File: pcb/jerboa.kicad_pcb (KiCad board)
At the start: 2 copper layers, 72 parts, among them IC1 ADP1607, IC2 MAX-M8Q, IC3 Si4460, IC4 BGS12AL7, J1 CONN_01x02, J2 CONN_01x03, J3 CONN_01x02, J4 CONN_01x02, P1 SWD_TC, P2 434MHz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

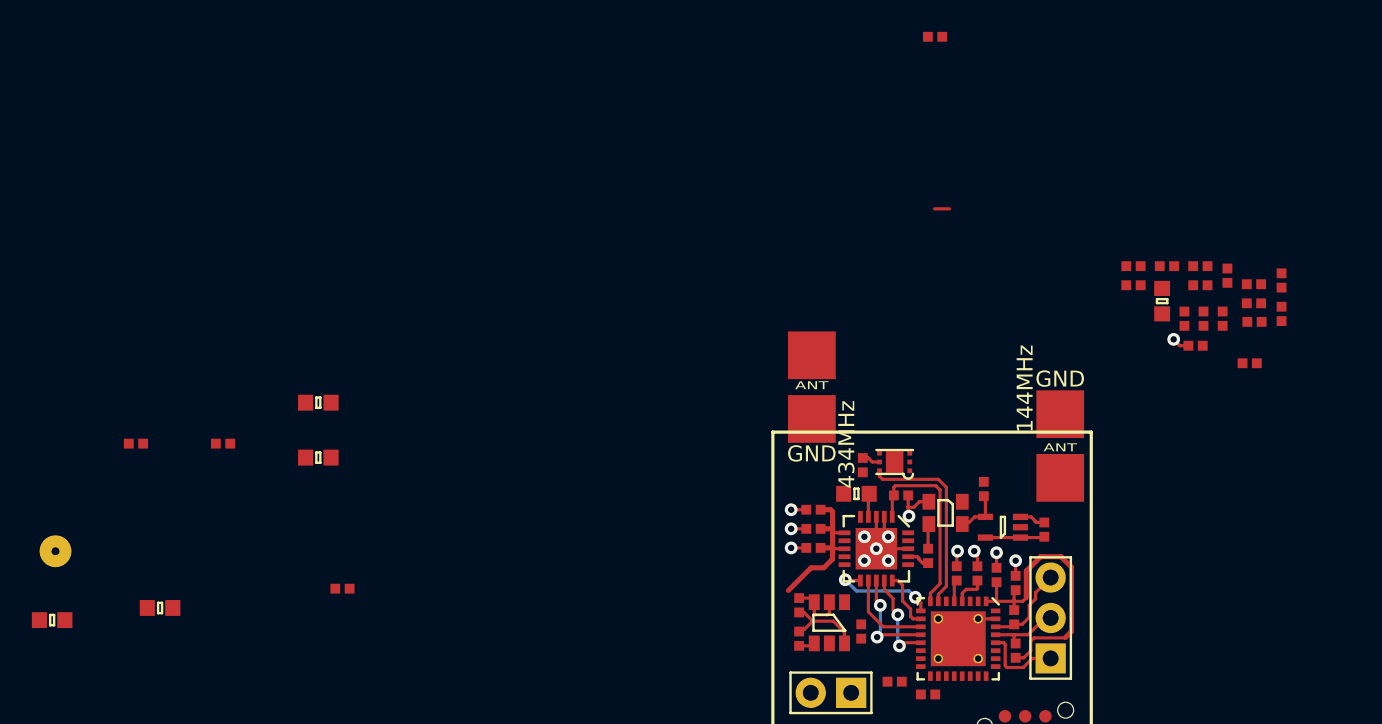
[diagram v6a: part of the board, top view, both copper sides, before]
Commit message: WIP: begin to place radio matching circuit on PCB
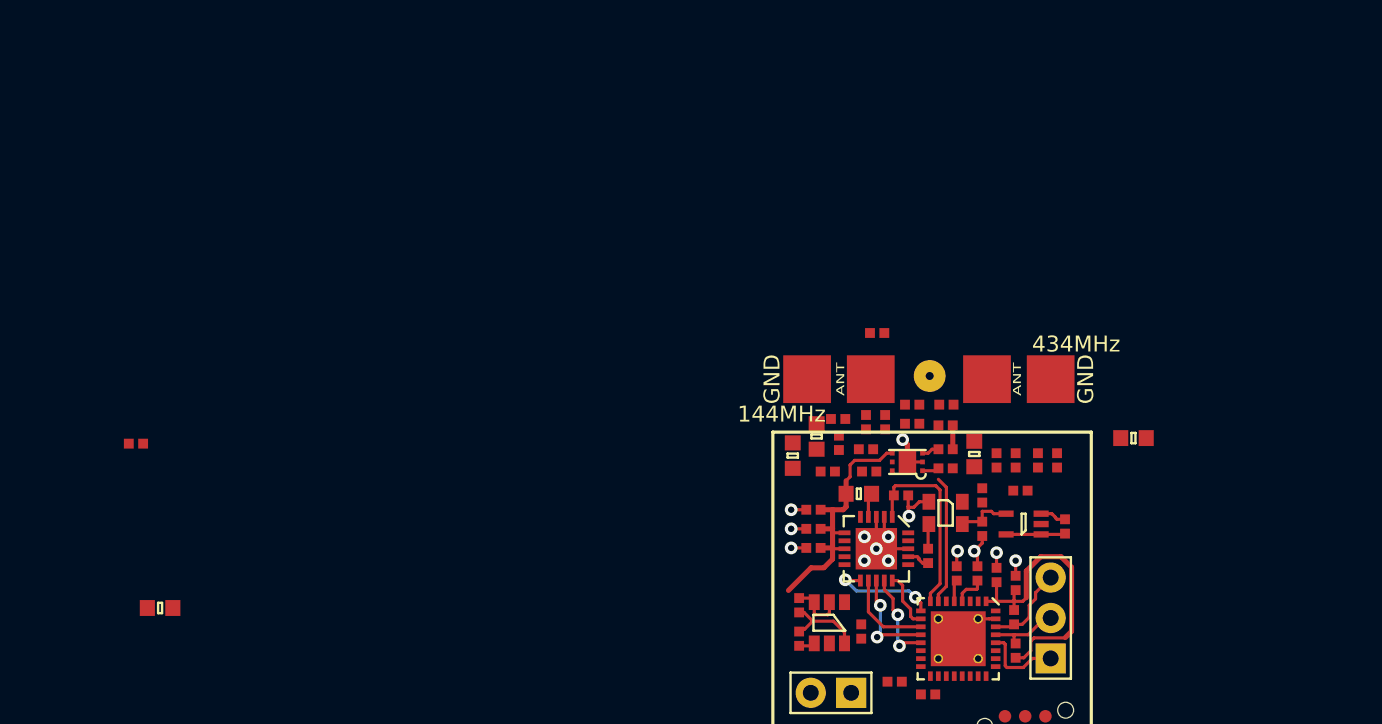
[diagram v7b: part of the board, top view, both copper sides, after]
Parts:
- moved TP1 56.0 mm to (142.0, 87.4)
- moved C35 51.2 mm to (154.8, 91.3)
- moved L13 49.4 mm to (134.9, 91.2), turned to 90 degrees
- moved D3 41.7 mm to (138.7, 84.7)
- moved C31 32.9 mm to (136.2, 90.1), turned to 180 degrees
- moved C33 30.9 mm to (135.6, 93.4), turned to 180 degrees
- moved C34 30.0 mm to (133.4, 92.4), turned to 90 degrees
- moved C13 29.0 mm to (145.3, 94.9), turned to 270 degrees
- moved C32 29.0 mm to (136.3, 91.6), turned to 270 degrees
- moved L12 25.7 mm to (138.0, 92.0)
- moved L11 25.5 mm to (138.0, 90.3), turned to 270 degrees
- moved C29 24.7 mm to (139.2, 90.3), turned to 270 degrees
- moved C28 21.4 mm to (140.9, 89.2), turned to 0 degrees
- moved L3 20.1 mm to (140.9, 90.4), turned to 180 degrees
- moved C26 18.2 mm to (143.1, 89.2), turned to 180 degrees
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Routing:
- net 3v3_switched: track 17.6 -> 24.3 mm
- net /FREQ_CTRL: track 12.2 -> 8.08 mm
- net GND: track 28.5 -> 30.1 mm
- net Net-(C23-Pad2): track 0.00 -> 1.50 mm
- net Net-(C20-Pad2): track 1.15 -> 0.00 mm
- net /radio/RADIO_TX_144: track 0.00 -> 1.10 mm
- net /radio/RADIO_TX_434: track 0.00 -> 1.06 mm

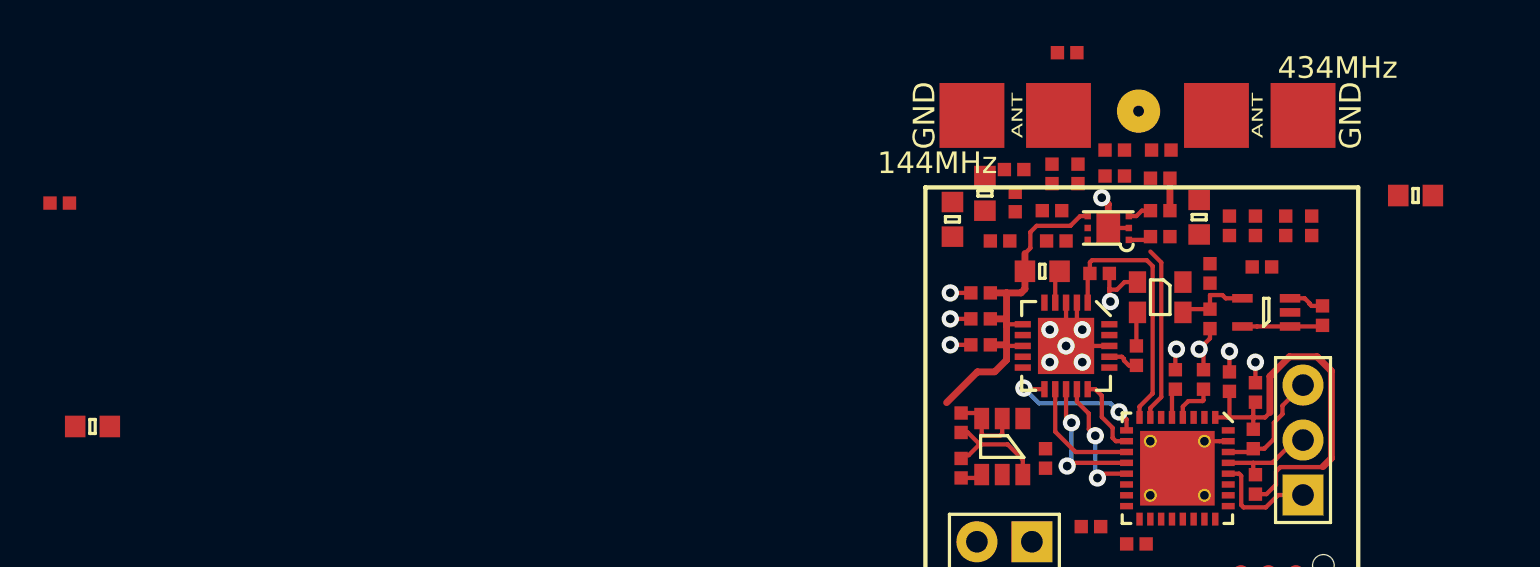
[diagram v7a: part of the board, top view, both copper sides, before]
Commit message: WIP: First attempt at routing 144MHz matching network
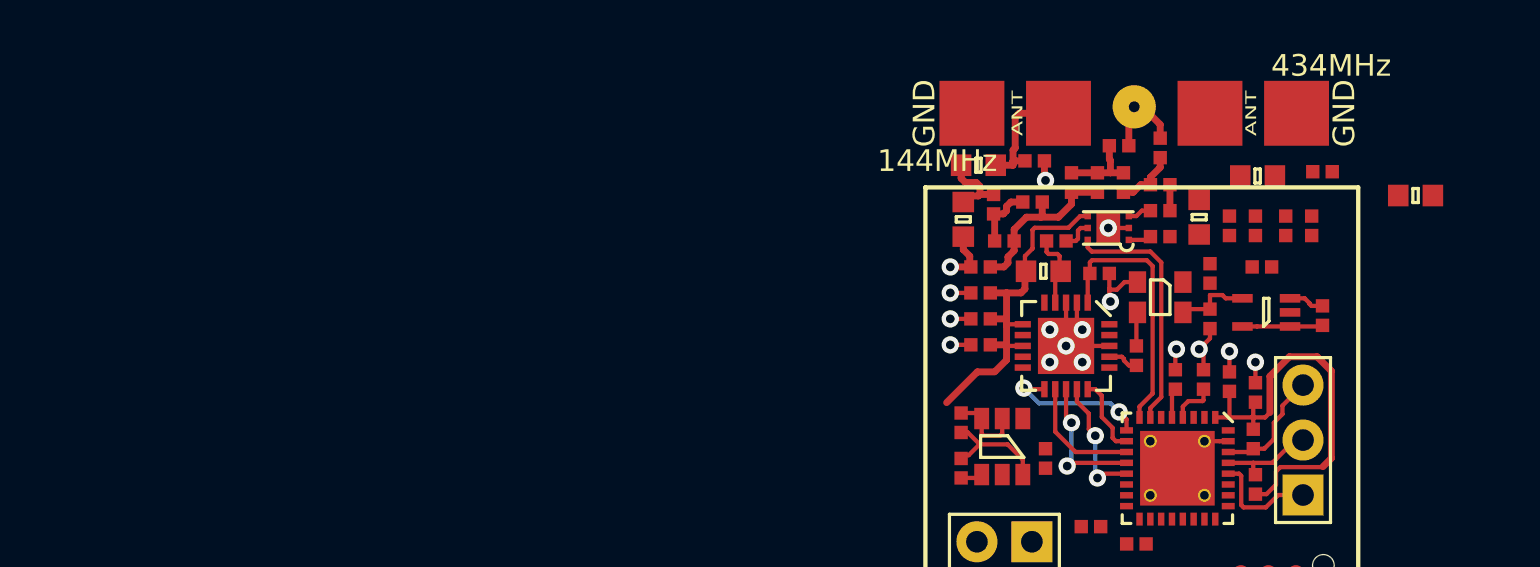
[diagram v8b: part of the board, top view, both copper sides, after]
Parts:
- moved D2 58.4 mm to (150.5, 90.2)
- moved L14 55.1 mm to (147.5, 90.4), turned to 180 degrees
- moved D3 5.22 mm to (137.2, 89.7)
- moved C31 4.76 mm to (134.7, 94.6)
- moved L11 2.14 mm to (140.1, 90.7)
- moved C32 1.87 mm to (135.8, 93.4), turned to 180 degrees
- moved C33 1.73 mm to (135.3, 91.7), turned to 90 degrees
- moved L13 1.33 mm to (134.6, 89.9), turned to 0 degrees
- moved L12 0.98 mm to (137.1, 91.6)
- moved L3 0.50 mm to (141.3, 90.7), turned to 90 degrees
- moved C34 0.50 mm to (133.9, 92.4), turned to 270 degrees
- moved C29 0.50 mm to (138.9, 90.7)
- moved P2 0.32 mm to (147.3, 87.5)
- moved L6 0.30 mm to (143.0, 90.8)
- moved C28 0.28 mm to (141.1, 89.0)
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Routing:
- net Net-(C29-Pad2): track 0.00 -> 8.17 mm
- net Net-(D3-Pad1): track 0.00 -> 6.53 mm
- net GND: track 30.1 -> 36.1 mm, vias 14 -> 16
- net Net-(C28-Pad1): track 0.00 -> 3.67 mm
- net Net-(C33-Pad2): track 0.00 -> 3.55 mm
- net /FREQ_CTRL: track 8.08 -> 11.4 mm
- net Net-(C32-Pad2): track 0.00 -> 3.18 mm
- net Net-(C26-Pad1): track 0.00 -> 2.83 mm
- net Net-(C20-Pad1): track 1.47 -> 3.42 mm
- net Net-(C20-Pad2): track 0.00 -> 1.47 mm
